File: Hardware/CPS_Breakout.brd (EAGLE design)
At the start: 11.6 x 11.6 mm, 9 parts

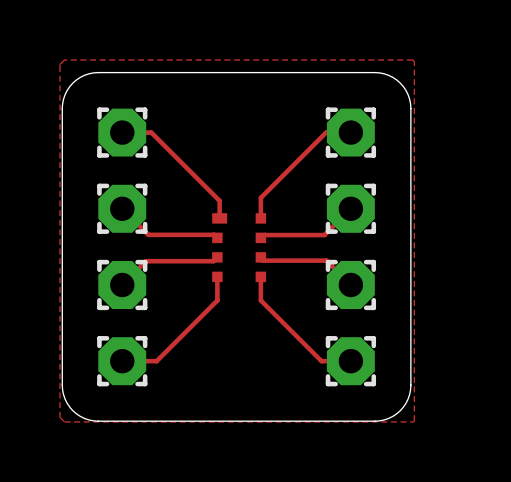
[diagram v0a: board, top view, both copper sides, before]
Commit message: updated pinheaders and names
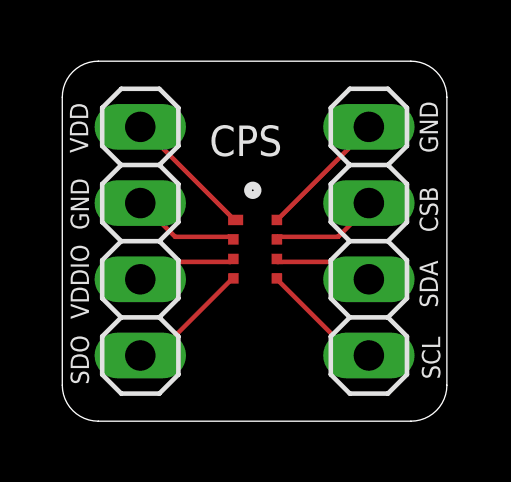
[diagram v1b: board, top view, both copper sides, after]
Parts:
- removed PAD1, PAD2, PAD3, PAD4, PAD5, PAD6, PAD7, PAD8: (no value), wirepad:1,6/0,8
- added JP1, JP2: (no value), pinhead:1X04
- moved B1 0.54 mm to (7.15, 4.76)
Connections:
- net N$1: now also B1.GND1, JP1.2; no longer B1.VDD, PAD1.1
- net N$2: now also B1.VDD, JP1.1; no longer B1.GND1, PAD2.1
- net N$3: now also JP1.3; no longer PAD3.1
- net N$4: now also JP1.4; no longer PAD4.1
- net N$5: now also JP2.1; no longer PAD5.1
- net N$6: now also JP2.2; no longer PAD6.1
- net N$7: now also JP2.3; no longer PAD7.1
- net N$8: now also JP2.4; no longer PAD8.1
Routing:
- net N$1: track 4.77 -> 3.58 mm
- net N$2: track 3.57 -> 4.46 mm
- net N$4: track 4.80 -> 4.16 mm
- removed copper zone on layer 1, net GND
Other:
- board size 11.6 x 11.6 mm -> 12.8 x 12 mm
- board text added: "CPS"
- board text added: "CSB"
- board text added: "GND"
- board text added: "SCL"
- board text added: "SDA"
- board text added: "SDO"
- board text added: "VDD"
- board text added: "VDDIO"
